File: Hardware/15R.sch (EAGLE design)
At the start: 666 parts, among them J2 USB Female Type C Connector, J3 AUDIO_JACK_TRRSSMD_RA, Q2 MBT3904DW1T1, U2 ESP-WROOM-32NARROW, U3 AP2112K-3.3V, U4 CP2102N, U5 ADMP401

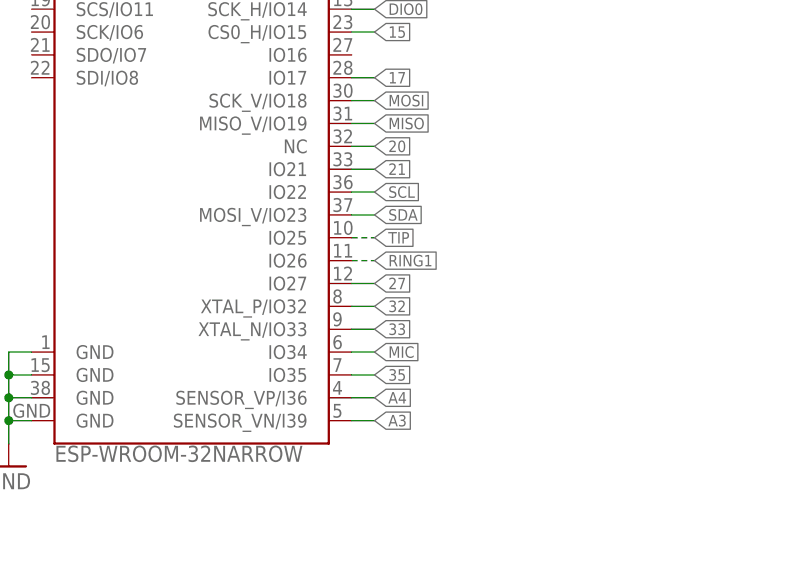
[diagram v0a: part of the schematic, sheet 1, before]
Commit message: adding in left/right for mic capability
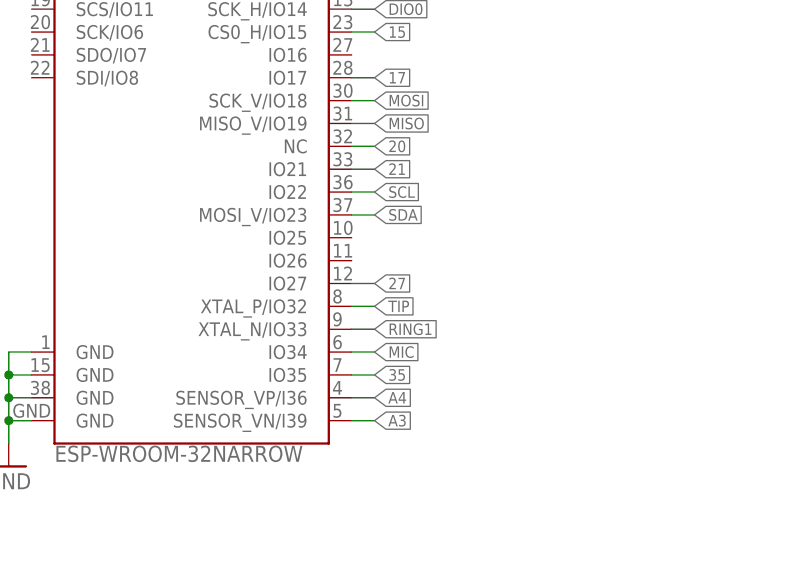
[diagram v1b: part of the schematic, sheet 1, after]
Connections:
- removed net 32: U2.XTAL_P/IO32
- removed net 33: U2.XTAL_N/IO33
- net RING1: now also U2.XTAL_N/IO33; no longer U2.IO26
- net TIP: now also U2.XTAL_P/IO32; no longer U2.IO25
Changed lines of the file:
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@@
 <?xml version="1.0" encoding="utf-8"?>
 <!DOCTYPE eagle SYSTEM "eagle.dtd">
-<eagle version="9.3.1">
+<eagle version="9.1.0">
 <drawing>
 <settings>
@@
 </segment>
 </net>
-<net name="32" class="0">
-<segment>
-<pinref part="U2" gate="G$1" pin="XTAL_P/IO32"/>
-<wire x1="134.62" y1="86.36" x2="137.16" y2="86.36" width="0.1524" layer="91"/>
-<label x="137.16" y="86.36" size="1.27" layer="95" xref="yes"/>
-</segment>
-</net>
 <net name="15" class="0">
 <segment>
@@
 <wire x1="134.62" y1="116.84" x2="137.16" y2="116.84" width="0.1524" layer="91"/>
 <label x="137.16" y="116.84" size="1.27" layer="95" xref="yes"/>
-</segment>
-</net>
-<net name="33" class="0">
-<segment>
-<pinref part="U2" gate="G$1" pin="XTAL_N/IO33"/>
-<wire x1="134.62" y1="83.82" x2="137.16" y2="83.82" width="0.1524" layer="91"/>
-<label x="137.16" y="83.82" size="1.27" layer="95" xref="yes"/>
 </segment>
 </net>
@@
 </segment>
 <segment>
-<pinref part="U2" gate="G$1" pin="IO26"/>
-<wire x1="134.62" y1="91.44" x2="137.16" y2="91.44" width="0.1524" layer="91" style="longdash"/>
-<label x="137.16" y="91.44" size="1.27" layer="95" font="vector" xref="yes"/>
+<pinref part="U2" gate="G$1" pin="XTAL_N/IO33"/>
+<wire x1="134.62" y1="83.82" x2="137.16" y2="83.82" width="0.1524" layer="91"/>
+<label x="137.16" y="83.82" size="1.27" layer="95" xref="yes"/>
 </segment>
 </net>
@@
 </segment>
 <segment>
-<pinref part="U2" gate="G$1" pin="IO25"/>
-<wire x1="134.62" y1="93.98" x2="137.16" y2="93.98" width="0.1524" layer="91" style="longdash"/>
-<label x="137.16" y="93.98" size="1.27" layer="95" font="vector" xref="yes"/>
-</segment>
-</net>
+<pinref part="U2" gate="G$1" pin="XTAL_P/IO32"/>
+<wire x1="134.62" y1="86.36" x2="137.16" y2="86.36" width="0.1524" layer="91"/>
+<label x="137.16" y="86.36" size="1.27" layer="95" xref="yes"/>
+</segment>
+</net>

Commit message: routing 15 inch
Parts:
- R13: value 1k -> 2.2k; device SparkFun-Resistors:1KOHM-HORIZ-1/4W-5% -> SparkFun-Resistors:2.2KOHM-0603-1/10W-1%
- R16: device SparkFun-Resistors:100OHM-0603-1/4W-5% -> SparkFun-Resistors:100OHM-0603-1/10W-1%
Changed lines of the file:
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@@
 <?xml version="1.0" encoding="utf-8"?>
 <!DOCTYPE eagle SYSTEM "eagle.dtd">
-<eagle version="9.1.0">
+<eagle version="9.5.2">
 <drawing>
 <settings>
@@
 <part name="C6" library="SparkFun-Capacitors" deviceset="1.0UF" device="-0603-16V-10%" value="1.0uF"/>
 <part name="GND13" library="SparkFun-PowerSymbols" deviceset="GND" device=""/>
-<part name="R13" library="SparkFun-Resistors" deviceset="1KOHM" device="-HORIZ-1/4W-5%" value="1k"/>
+<part name="R13" library="SparkFun-Resistors" deviceset="2.2KOHM" device="-0603-1/10W-1%" value="2.2k"/>
 <part name="C9" library="SparkFun-Capacitors" deviceset="0.1UF" device="-0603-25V-5%" value="0.1uF"/>
 <part name="R11" library="SparkFun-Resistors" deviceset="100KOHM" device="-0603-1/10W-1%" value="100k"/>
@@
 <part name="GND277" library="SparkFun-PowerSymbols" deviceset="GND" device=""/>
 <part name="JP261" library="SparkFun-Jumpers" deviceset="JUMPER-SMT_2_NO" device="_NO-SILK" value="JUMPER-SMT_2_NO_NO-SILK"/>
-<part name="R16" library="SparkFun-Resistors" deviceset="100OHM" device="-0603-1/4W-5%" value="100"/>
+<part name="R16" library="SparkFun-Resistors" deviceset="100OHM" device="-0603-1/10W-1%" value="100"/>
 <part name="H1" library="SparkFun-Hardware" deviceset="STAND-OFF" device=""/>
 <part name="H2" library="SparkFun-Hardware" deviceset="STAND-OFF" device=""/>

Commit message: updating 13 inch, finish layout of 15 inch
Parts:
- removed D249: WS2812B, SparkFun-LED:WS2812B
- removed FRAME1, FRAME2, FRAME3, FRAME4: FRAME-LEDGER, SparkFun-Aesthetics:FRAME-LEDGER
- removed JP249: JUMPER-SMT_2_NO_NO-SILK, SparkFun-Jumpers:JUMPER-SMT_2_NO_NO-SILK
- added D309, D310, D311, D315: WS2812B, SparkFun-LED:WS2812B
- added JP309, JP310, JP311, JP315: JUMPER-SMT_2_NO_NO-SILK, SparkFun-Jumpers:JUMPER-SMT_2_NO_NO-SILK
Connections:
- removed net DIO120: D231.DO, D232.DI, JP231.2, JP232.1
- removed net DIO131: D248.DO, D249.DI, JP248.2, JP249.1
- new net DIO143: D309.DO, D310.DI, JP309.2, JP310.1
- new net DIO153: D232.DI, D315.DO, JP232.1, JP315.2
- new net N$170: D310.DO, D311.DI, JP310.2, JP311.1
- new net N$172: D231.DO, D309.DI, JP231.2, JP309.1
- new net N$173: D311.DO, D315.DI, JP311.2, JP315.1
- net DIO152: now also D248.DI, JP248.1; no longer D212.DI, JP212.1
- net GND: now also D309.VSS, D310.VSS, D311.VSS, D315.VSS; no longer D249.VSS
- net N$125: now also D212.DI, D248.DO, JP212.1, JP248.2; no longer D247.DO, D248.DI, JP247.2, JP248.1
- net N$128: now also D247.DO, JP247.2; no longer D249.DO, JP249.2
- net V_USB: now also D309.VDD, D310.VDD, D311.VDD, D315.VDD; no longer D249.VDD
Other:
- moved on the sheet: D248, JP248

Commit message: getting 4 boards polished
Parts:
- removed D11, D12, D13: WS2812B, SparkFun-LED:WS2812B
- removed JP11, JP12, JP13: JUMPER-SMT_2_NO_NO-SILK, SparkFun-Jumpers:JUMPER-SMT_2_NO_NO-SILK
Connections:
- removed net DIO5: D10.DO, D11.DI, JP10.2, JP11.1
- removed net DIO6: D13.DO, D14.DI, JP13.2, JP14.1
- removed net N$135: D11.DO, D12.DI, JP11.2, JP12.1
- net GND: no longer D11.VSS, D12.VSS, D13.VSS
- net N$8: now also D10.DO, D14.DI, JP10.2, JP14.1; no longer D12.DO, D13.DI, JP12.2, JP13.1
- net V_USB: no longer D11.VDD, D12.VDD, D13.VDD

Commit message: final touches, polishing, jumpers, CAM on all boards
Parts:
- added JP11, JP12, JP13, JP249, JP312, JP313, JP314, JP316, JP317, JP318, JP319, JP320, JP321: JUMPER-SMT_2_NO_NO-SILK, SparkFun-Jumpers:JUMPER-SMT_2_NO_NO-SILK
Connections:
- removed net DIO10: D211.DO, D22.DI, JP211.2, JP22.1
- removed net DIO109: D21.DI, D210.DO, JP1.1, JP210.2
- removed net DIO152: D248.DI, D308.DO, JP248.1, JP308.2
- removed net DIO99: D189.DO, D190.DI, JP189.2, JP190.1
- removed net N$128: D247.DO, D250.DI, JP247.2, JP250.1
- removed net N$139: D264.DO, D43.DI, JP264.2, JP43.1
- removed net N$140: D266.DO, D64.DI, JP266.2, JP64.1
- removed net N$144: D106.DI, D270.DO, JP106.1, JP270.2
- removed net N$147: D148.DI, D274.DO, JP148.1, JP274.2
- removed net N$172: D231.DO, D309.DI, JP231.2, JP309.1
- removed net N$54: D84.DO, D85.DI, JP84.2, JP85.1
- removed net N$68: D127.DI, D272.DO, JP127.1, JP272.2
- removed net N$89: D168.DO, D169.DI, JP168.2, JP169.1
- new net JUMPER0: D211.DO, D22.DI, JP11.2, JP12.1, JP211.2, JP22.1
- new net JUMPER1: D264.DO, D43.DI, JP12.2, JP13.1, JP264.2, JP43.1
- new net JUMPER10: D248.DI, D308.DO, JP248.1, JP308.2, JP319.2, JP320.1
- new net JUMPER11: D231.DO, D309.DI, JP231.2, JP309.1, JP320.2, JP321.1
- new net JUMPER12: D247.DO, D250.DI, JP247.2, JP250.1, JP321.2
- new net JUMPER2: D266.DO, D64.DI, JP13.2, JP249.1, JP266.2, JP64.1
- new net JUMPER3: D84.DO, D85.DI, JP249.2, JP312.1, JP84.2, JP85.1
- new net JUMPER4: D106.DI, D270.DO, JP106.1, JP270.2, JP312.2, JP313.1
- new net JUMPER5: D127.DI, D272.DO, JP127.1, JP272.2, JP313.2, JP314.1
- new net JUMPER6: D148.DI, D274.DO, JP148.1, JP274.2, JP314.2, JP316.1
- new net JUMPER7: D168.DO, D169.DI, JP168.2, JP169.1, JP316.2, JP317.1
- new net JUMPER8: D189.DO, D190.DI, JP189.2, JP190.1, JP317.2, JP318.1
- new net JUMPER9: D21.DI, D210.DO, JP1.1, JP210.2, JP318.2, JP319.1
- net DIO0: now also JP11.1

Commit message: pushing final board changes
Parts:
- removed D309, D310, D311: WS2812B, SparkFun-LED:WS2812B
- removed JP309, JP310, JP311: JUMPER-SMT_2_NO_NO-SILK, SparkFun-Jumpers:JUMPER-SMT_2_NO_NO-SILK
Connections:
- removed net DIO143: D309.DO, D310.DI, JP309.2, JP310.1
- removed net N$170: D310.DO, D311.DI, JP310.2, JP311.1
- removed net N$173: D311.DO, D315.DI, JP311.2, JP315.1
- net GND: no longer D309.VSS, D310.VSS, D311.VSS
- net JUMPER11: now also D315.DI, JP315.1; no longer D309.DI, JP309.1
- net V_USB: no longer D309.VDD, D310.VDD, D311.VDD

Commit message: updating files
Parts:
- removed FD1: FIDUCIALUFIDUCIAL, SparkFun-Aesthetics:FIDUCIALUFIDUCIAL
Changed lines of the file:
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@@
 <part name="GND3" library="SparkFun-Aesthetics" deviceset="GND" device=""/>
 <part name="C1" library="SparkFun-Capacitors" deviceset="10UF" device="-0603-6.3V-20%" value="10uF"/>
-<part name="FD1" library="SparkFun-Aesthetics" deviceset="FIDUCIAL" device="UFIDUCIAL"/>
 <part name="FD2" library="SparkFun-Aesthetics" deviceset="FIDUCIAL" device="UFIDUCIAL"/>
 <part name="FD4" library="SparkFun-Aesthetics" deviceset="FIDUCIAL" device="UFIDUCIAL"/>
@@
 <attribute name="VALUE" x="110.744" y="231.521" size="1.778" layer="96" font="vector"/>
 </instance>
-<instance part="FD1" gate="G$1" x="429.26" y="33.02" smashed="yes"/>
 <instance part="FD2" gate="G$1" x="426.72" y="33.02" smashed="yes"/>
 <instance part="FD4" gate="G$1" x="429.26" y="30.48" smashed="yes"/>
